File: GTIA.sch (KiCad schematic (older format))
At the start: 78 parts, among them J102 pin, J103 pin, J104 pin, J105 pin, J2 Video, J202 Diag, J210 Diag, Q1 2N3904, Q2 2N3904, Q3 2N3904, Q6 2N3904, U17 GTIA, U18 74LS08, U20 4050, U21 74LS74, Y2 4,43 MHz

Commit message: Basic smd
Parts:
- removed R205: 150, Atari:R_Axial_DIN0207_L3.6mm_D2.2mm_P10.16mm_Horizontal, symbol Device:R
- added D1000: 1N4002, Diode_THT:D_DO-41_SOD81_P12.70mm_Horizontal, symbol Diode:1N4002
- C42: footprint Atari:C_Axial_L5.1mm_D2.5mm_P12.50mm_Horizontal -> Capacitor_SMD:C_1206_3216Metric_Pad1.42x1.75mm_HandSolder
- C50: value 10uF -> 220uF
- R116: value 51 -> 8,2
- R202: value 180 -> 75
- R204: value 47 -> 75
- R53: value 100 -> 75
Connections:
- net at Q2.1 (E), R202.2: now also D1000.2 (A)
- net at FB31.2: now also D1000.1 (K)
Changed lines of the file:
@@
 F 0 "C42" H 4840 4771 50  0000 L CNN
 F 1 "100nF" H 4840 4680 50  0000 L CNN
-F 2 "Atari:C_Axial_L5.1mm_D2.5mm_P12.50mm_Horizontal" H 4763 4575 50  0001 C CNN
+F 2 "Capacitor_SMD:C_1206_3216Metric_Pad1.42x1.75mm_HandSolder" H 4763 4575 50  0001 C CNN
 F 3 "~" H 4725 4725 50  0001 C CNN
 	1    4725 4725
@@
 P 7425 850
 F 0 "C50" H 7543 896 50  0000 L CNN
-F 1 "10uF" H 7543 805 50  0000 L CNN
+F 1 "220uF" H 7543 805 50  0000 L CNN
 F 2 "Capacitor_THT:CP_Radial_D5.0mm_P2.00mm" H 7463 700 50  0001 C CNN
 F 3 "~" H 7425 850 50  0001 C CNN
@@
 P 9300 1125
 F 0 "R116" V 9225 1025 50  0000 L CNN
-F 1 "51" H 9350 1125 50  0000 L CNN
+F 1 "8,2" H 9350 1125 50  0000 L CNN
 F 2 "Atari:R_Axial_DIN0207_L3.6mm_D2.2mm_P10.16mm_Horizontal" V 9230 1125 50  0001 C CNN
 F 3 "~" H 9300 1125 50  0001 C CNN
@@
 P 9300 2125
 F 0 "R53" V 9300 2050 50  0000 L CNN
-F 1 "100" H 9350 2125 50  0000 L CNN
+F 1 "75" H 9350 2125 50  0000 L CNN
 F 2 "Atari:R_Axial_DIN0207_L3.6mm_D2.2mm_P10.16mm_Horizontal" V 9230 2125 50  0001 C CNN
 F 3 "~" H 9300 2125 50  0001 C CNN
@@
 P 9825 1900
 F 0 "R204" V 9750 1900 50  0000 C CNN
-F 1 "47" V 9925 1900 50  0000 C CNN
+F 1 "75" V 9925 1900 50  0000 C CNN
 F 2 "Atari:R_Axial_DIN0207_L3.6mm_D2.2mm_P10.16mm_Horizontal" V 9755 1900 50  0001 C CNN
 F 3 "~" H 9825 1900 50  0001 C CNN
@@
 P 8025 3950
 F 0 "R202" V 8025 3950 50  0000 C CNN
-F 1 "180" V 7909 3950 50  0000 C CNN
+F 1 "75" V 7909 3950 50  0000 C CNN
 F 2 "Atari:R_Axial_DIN0207_L3.6mm_D2.2mm_P10.16mm_Horizontal" V 7955 3950 50  0001 C CNN
 F 3 "~" H 8025 3950 50  0001 C CNN
 	1    8025 3950
 	-1   0    0    1
-$EndComp
-$Comp
-L Device:R R205
-U 1 1 604741B6
-P 8450 3625
-F 0 "R205" V 8450 3625 50  0000 C CNN
-F 1 "150" V 8334 3625 50  0000 C CNN
-F 2 "Atari:R_Axial_DIN0207_L3.6mm_D2.2mm_P10.16mm_Horizontal" V 8380 3625 50  0001 C CNN
-F 3 "~" H 8450 3625 50  0001 C CNN
-	1    8450 3625
-	0    1    1    0
 $EndComp
 Wire Wire Line
@@
 Wire Wire Line
 	3350 7300 3350 7500
+$Comp
+L Diode:1N4002 D1000
+U 1 1 623E583A
+P 8450 3625
+F 0 "D1000" H 8450 3409 50  0000 C CNN
+F 1 "1N4002" H 8450 3500 50  0000 C CNN
+F 2 "Diode_THT:D_DO-41_SOD81_P12.70mm_Horizontal" H 8450 3450 50  0001 C CNN
+F 3 "http://www.vishay.com/docs/88503/1n4001.pdf" H 8450 3625 50  0001 C CNN
+	1    8450 3625
+	-1   0    0    1
+$EndComp
 $EndSCHEMATC

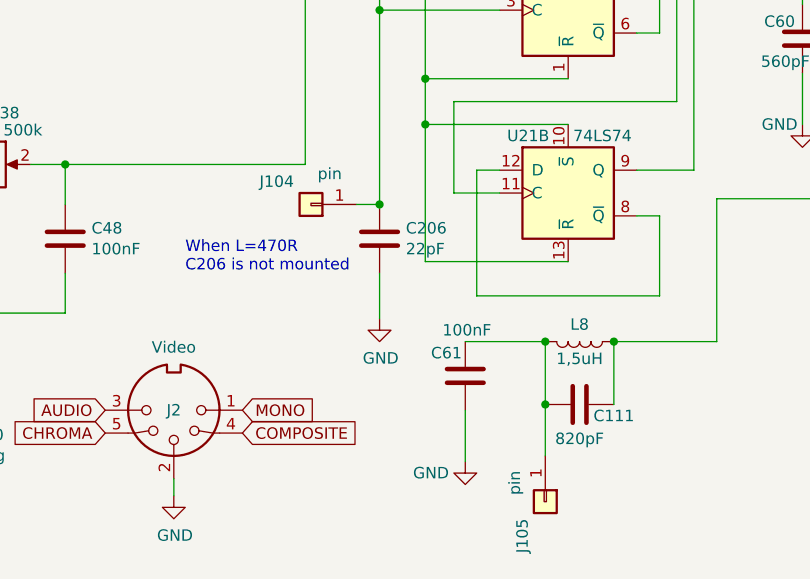
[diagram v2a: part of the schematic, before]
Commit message: PAL to smd
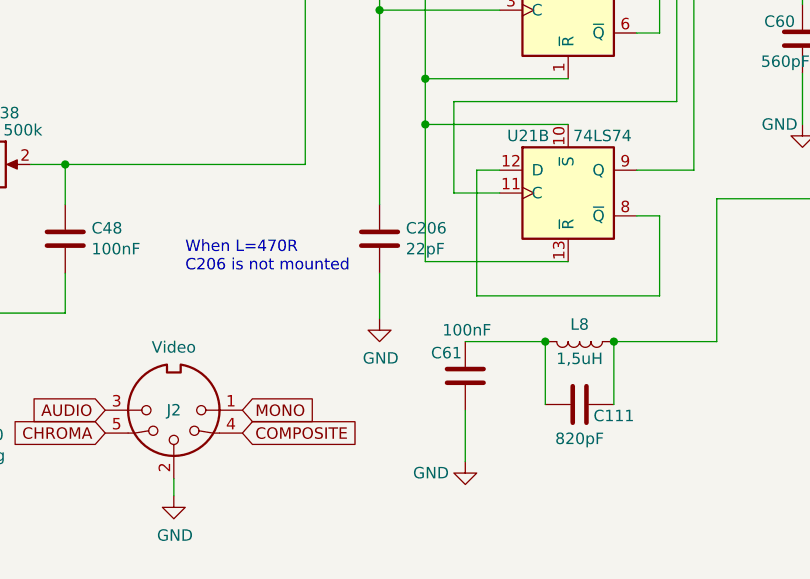
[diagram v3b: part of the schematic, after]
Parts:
- removed J104, J105: pin, Connector_PinHeader_2.00mm:PinHeader_1x01_P2.00mm_Vertical, symbol Connector_Generic:Conn_01x01
- C111, C206, C58, C59, C60, C61: footprint Atari:C_Axial_L5.1mm_D2.5mm_P12.50mm_Horizontal -> Capacitor_SMD:C_1206_3216Metric_Pad1.42x1.75mm_HandSolder
- L37: footprint Atari:L_Axial_L7.0mm_D3.3mm_P12.50mm_Horizontal_Fastron_MICC -> Capacitor_SMD:C_1206_3216Metric_Pad1.42x1.75mm_HandSolder
- L8: footprint Atari:L_Axial_L7.0mm_D3.3mm_P12.50mm_Horizontal_Fastron_MICC -> Inductor_SMD:L_1812_4532Metric_Pad1.30x3.40mm_HandSolder
- R69, R70, R71, R72, R73: footprint Atari:R_Axial_DIN0207_L3.6mm_D2.2mm_P10.16mm_Horizontal -> Resistor_SMD:R_1206_3216Metric_Pad1.42x1.75mm_HandSolder
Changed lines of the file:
@@
 F 0 "C206" H 5310 6354 50  0000 R CNN
 F 1 "22pF" H 5310 6445 50  0000 R CNN
-F 2 "Atari:C_Axial_L5.1mm_D2.5mm_P12.50mm_Horizontal" H 5463 6250 50  0001 C CNN
+F 2 "Capacitor_SMD:C_1206_3216Metric_Pad1.42x1.75mm_HandSolder" H 5463 6250 50  0001 C CNN
 F 3 "~" H 5425 6400 50  0001 C CNN
 	1    5425 6400
@@
 F 0 "L37" V 3725 5200 50  0000 C CNN
 F 1 "Bead or 470R" V 3900 5200 50  0000 C CNN
-F 2 "Atari:L_Axial_L7.0mm_D3.3mm_P12.50mm_Horizontal_Fastron_MICC" H 3800 5200 50  0001 C CNN
+F 2 "Capacitor_SMD:C_1206_3216Metric_Pad1.42x1.75mm_HandSolder" H 3800 5200 50  0001 C CNN
 F 3 "~" H 3800 5200 50  0001 C CNN
 	1    3800 5200
@@
 F 0 "R73" H 7345 5021 50  0000 L CNN
 F 1 "4k7" H 7345 4930 50  0000 L CNN
-F 2 "Atari:R_Axial_DIN0207_L3.6mm_D2.2mm_P10.16mm_Horizontal" V 7205 4975 50  0001 C CNN
+F 2 "Resistor_SMD:R_1206_3216Metric_Pad1.42x1.75mm_HandSolder" V 7205 4975 50  0001 C CNN
 F 3 "~" H 7275 4975 50  0001 C CNN
 	1    7275 4975
@@
 F 0 "C60" H 7375 5450 50  0000 C CNN
 F 1 "560pF" H 7350 5625 50  0000 C CNN
-F 2 "Atari:C_Axial_L5.1mm_D2.5mm_P12.50mm_Horizontal" H 7313 5375 50  0001 C CNN
+F 2 "Capacitor_SMD:C_1206_3216Metric_Pad1.42x1.75mm_HandSolder" H 7313 5375 50  0001 C CNN
 F 3 "~" H 7275 5525 50  0001 C CNN
 	1    7275 5525
@@
 F 0 "C59" V 7850 5250 50  0000 C CNN
 F 1 "22pF" V 7550 5250 50  0000 C CNN
-F 2 "Atari:C_Axial_L5.1mm_D2.5mm_P12.50mm_Horizontal" H 7738 5100 50  0001 C CNN
+F 2 "Capacitor_SMD:C_1206_3216Metric_Pad1.42x1.75mm_HandSolder" H 7738 5100 50  0001 C CNN
 F 3 "~" H 7700 5250 50  0001 C CNN
 	1    7700 5250
@@
 F 0 "R70" H 9445 4996 50  0000 L CNN
 F 1 "10k" H 9445 4905 50  0000 L CNN
-F 2 "Atari:R_Axial_DIN0207_L3.6mm_D2.2mm_P10.16mm_Horizontal" V 9305 4950 50  0001 C CNN
+F 2 "Resistor_SMD:R_1206_3216Metric_Pad1.42x1.75mm_HandSolder" V 9305 4950 50  0001 C CNN
 F 3 "~" H 9375 4950 50  0001 C CNN
 	1    9375 4950
@@
 F 0 "R69" H 9445 5571 50  0000 L CNN
 F 1 "6k8" H 9445 5480 50  0000 L CNN
-F 2 "Atari:R_Axial_DIN0207_L3.6mm_D2.2mm_P10.16mm_Horizontal" V 9305 5525 50  0001 C CNN
+F 2 "Resistor_SMD:R_1206_3216Metric_Pad1.42x1.75mm_HandSolder" V 9305 5525 50  0001 C CNN
 F 3 "~" H 9375 5525 50  0001 C CNN
 	1    9375 5525
@@
 F 0 "R71" V 8868 5250 50  0000 C CNN
 F 1 "470" V 8959 5250 50  0000 C CNN
-F 2 "Atari:R_Axial_DIN0207_L3.6mm_D2.2mm_P10.16mm_Horizontal" V 9005 5250 50  0001 C CNN
+F 2 "Resistor_SMD:R_1206_3216Metric_Pad1.42x1.75mm_HandSolder" V 9005 5250 50  0001 C CNN
 F 3 "~" H 9075 5250 50  0001 C CNN
 	1    9075 5250
@@
 F 0 "R72" V 9568 4425 50  0000 C CNN
 F 1 "1k" V 9659 4425 50  0000 C CNN
-F 2 "Atari:R_Axial_DIN0207_L3.6mm_D2.2mm_P10.16mm_Horizontal" V 9705 4425 50  0001 C CNN
+F 2 "Resistor_SMD:R_1206_3216Metric_Pad1.42x1.75mm_HandSolder" V 9705 4425 50  0001 C CNN
 F 3 "~" H 9775 4425 50  0001 C CNN
 	1    9775 4425
@@
 F 0 "L8" V 6225 6850 50  0000 C CNN
 F 1 "1,5uH" V 6375 6850 50  0000 C CNN
-F 2 "Atari:L_Axial_L7.0mm_D3.3mm_P12.50mm_Horizontal_Fastron_MICC" H 6300 6850 50  0001 C CNN
+F 2 "Inductor_SMD:L_1812_4532Metric_Pad1.30x3.40mm_HandSolder" H 6300 6850 50  0001 C CNN
 F 3 "~" H 6300 6850 50  0001 C CNN
 	1    6300 6850
@@
 F 0 "C111" V 6350 7275 50  0000 C CNN
 F 1 "820pF" V 6450 7125 50  0000 C CNN
-F 2 "Atari:C_Axial_L5.1mm_D2.5mm_P12.50mm_Horizontal" H 6338 6975 50  0001 C CNN
+F 2 "Capacitor_SMD:C_1206_3216Metric_Pad1.42x1.75mm_HandSolder" H 6338 6975 50  0001 C CNN
 F 3 "~" H 6300 7125 50  0001 C CNN
 	1    6300 7125
@@
 F 0 "C61" H 5950 6900 50  0000 R CNN
 F 1 "100nF" H 5900 6800 50  0000 R CNN
-F 2 "Atari:C_Axial_L5.1mm_D2.5mm_P12.50mm_Horizontal" H 5838 6850 50  0001 C CNN
+F 2 "Capacitor_SMD:C_1206_3216Metric_Pad1.42x1.75mm_HandSolder" H 5838 6850 50  0001 C CNN
 F 3 "~" H 5800 7000 50  0001 C CNN
 	1    5800 7000
@@
 F 0 "C58" H 1790 3671 50  0000 L CNN
 F 1 "100nF" H 1790 3580 50  0000 L CNN
-F 2 "Atari:C_Axial_L5.1mm_D2.5mm_P12.50mm_Horizontal" H 1713 3475 50  0001 C CNN
+F 2 "Capacitor_SMD:C_1206_3216Metric_Pad1.42x1.75mm_HandSolder" H 1713 3475 50  0001 C CNN
 F 3 "~" H 1675 3625 50  0001 C CNN
 	1    1675 3625
@@
 Wire Wire Line
 	2375 6200 2375 6000
-$Comp
-L Connector_Generic:Conn_01x01 J104
-U 1 1 603FEA4A
-P 5125 6250
-F 0 "J104" H 5275 6150 50  0000 C CNN
-F 1 "pin" H 5043 6116 50  0000 C CNN
-F 2 "Connector_PinHeader_2.00mm:PinHeader_1x01_P2.00mm_Vertical" H 5125 6250 50  0001 C CNN
-F 3 "~" H 5125 6250 50  0001 C CNN
-	1    5125 6250
-	-1   0    0    1
-$EndComp
-Wire Wire Line
-	5325 6250 5425 6250
-Connection ~ 5425 6250
-$Comp
-L Connector_Generic:Conn_01x01 J105
-U 1 1 6041A994
-P 6150 7550
-F 0 "J105" H 6300 7450 50  0000 C CNN
-F 1 "pin" H 6068 7416 50  0000 C CNN
-F 2 "Connector_PinHeader_2.00mm:PinHeader_1x01_P2.00mm_Vertical" H 6150 7550 50  0001 C CNN
-F 3 "~" H 6150 7550 50  0001 C CNN
-	1    6150 7550
-	0    1    1    0
-$EndComp
-Wire Wire Line
-	6150 7350 6150 7125
-Connection ~ 6150 7125
 Text GLabel 2650 7200 0    50   Input ~ 0
 MONO

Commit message: ROM refactoring
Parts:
- removed J102, J103: pin, Connector_PinHeader_2.00mm:PinHeader_1x01_P2.00mm_Vertical, symbol Connector_Generic:Conn_01x01
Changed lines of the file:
@@
 	1    0    0    -1
 $EndComp
-$Comp
-L Connector_Generic:Conn_01x01 J102
-U 1 1 6037C604
-P 800 6575
-F 0 "J102" H 950 6475 50  0000 C CNN
-F 1 "pin" H 718 6441 50  0000 C CNN
-F 2 "Connector_PinHeader_2.00mm:PinHeader_1x01_P2.00mm_Vertical" H 800 6575 50  0001 C CNN
-F 3 "~" H 800 6575 50  0001 C CNN
-	1    800  6575
-	-1   0    0    1
-$EndComp
-Wire Wire Line
-	1000 6575 1200 6575
-Wire Wire Line
-	1200 6575 1200 6200
-$Comp
-L Connector_Generic:Conn_01x01 J103
-U 1 1 603DC950
-P 2375 6400
-F 0 "J103" H 2525 6300 50  0000 C CNN
-F 1 "pin" H 2293 6266 50  0000 C CNN
-F 2 "Connector_PinHeader_2.00mm:PinHeader_1x01_P2.00mm_Vertical" H 2375 6400 50  0001 C CNN
-F 3 "~" H 2375 6400 50  0001 C CNN
-	1    2375 6400
-	0    1    1    0
-$EndComp
-Wire Wire Line
-	2375 6200 2375 6000
 Text GLabel 2650 7200 0    50   Input ~ 0
 MONO

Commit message: SMD continue
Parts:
- C204, C51: footprint Atari:C_Axial_L5.1mm_D2.5mm_P12.50mm_Horizontal -> Capacitor_SMD:C_1206_3216Metric_Pad1.42x1.75mm_HandSolder
- D1000: footprint Diode_THT:D_DO-41_SOD81_P12.70mm_Horizontal -> Diode_SMD:D_MELF_Handsoldering
- FB31, L32, L5, L6: footprint Atari:L_Axial_L7.0mm_D3.3mm_P12.50mm_Horizontal_Fastron_MICC -> Inductor_SMD:L_1812_4532Metric_Pad1.30x3.40mm_HandSolder
- R201, R202, R203, R41, R42, R43, R44, R45: footprint Atari:R_Axial_DIN0207_L3.6mm_D2.2mm_P10.16mm_Horizontal -> Resistor_SMD:R_1206_3216Metric_Pad1.42x1.75mm_HandSolder
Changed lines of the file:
@@
 F 0 "R41" V 6225 1100 50  0000 L CNN
 F 1 "1k" H 6275 1175 50  0000 L CNN
-F 2 "Atari:R_Axial_DIN0207_L3.6mm_D2.2mm_P10.16mm_Horizontal" V 6155 1175 50  0001 C CNN
+F 2 "Resistor_SMD:R_1206_3216Metric_Pad1.42x1.75mm_HandSolder" V 6155 1175 50  0001 C CNN
 F 3 "~" H 6225 1175 50  0001 C CNN
 	1    6225 1175
@@
 F 0 "R42" V 6025 1100 50  0000 L CNN
 F 1 "1k" H 6075 1175 50  0000 L CNN
-F 2 "Atari:R_Axial_DIN0207_L3.6mm_D2.2mm_P10.16mm_Horizontal" V 5955 1175 50  0001 C CNN
+F 2 "Resistor_SMD:R_1206_3216Metric_Pad1.42x1.75mm_HandSolder" V 5955 1175 50  0001 C CNN
 F 3 "~" H 6025 1175 50  0001 C CNN
 	1    6025 1175
@@
 F 0 "R43" V 5825 1100 50  0000 L CNN
 F 1 "1k" H 5875 1175 50  0000 L CNN
-F 2 "Atari:R_Axial_DIN0207_L3.6mm_D2.2mm_P10.16mm_Horizontal" V 5755 1175 50  0001 C CNN
+F 2 "Resistor_SMD:R_1206_3216Metric_Pad1.42x1.75mm_HandSolder" V 5755 1175 50  0001 C CNN
 F 3 "~" H 5825 1175 50  0001 C CNN
 	1    5825 1175
@@
 F 0 "R44" V 5625 1100 50  0000 L CNN
 F 1 "1k" H 5675 1175 50  0000 L CNN
-F 2 "Atari:R_Axial_DIN0207_L3.6mm_D2.2mm_P10.16mm_Horizontal" V 5555 1175 50  0001 C CNN
+F 2 "Resistor_SMD:R_1206_3216Metric_Pad1.42x1.75mm_HandSolder" V 5555 1175 50  0001 C CNN
 F 3 "~" H 5625 1175 50  0001 C CNN
 	1    5625 1175
@@
 F 0 "R45" V 5425 1100 50  0000 L CNN
 F 1 "1k" H 5475 1175 50  0000 L CNN
-F 2 "Atari:R_Axial_DIN0207_L3.6mm_D2.2mm_P10.16mm_Horizontal" V 5355 1175 50  0001 C CNN
+F 2 "Resistor_SMD:R_1206_3216Metric_Pad1.42x1.75mm_HandSolder" V 5355 1175 50  0001 C CNN
 F 3 "~" H 5425 1175 50  0001 C CNN
 	1    5425 1175
@@
 F 0 "L5" V 6750 700 50  0000 C CNN
 F 1 "820uH" V 6900 700 50  0000 C CNN
-F 2 "Atari:L_Axial_L7.0mm_D3.3mm_P12.50mm_Horizontal_Fastron_MICC" H 6825 700 50  0001 C CNN
+F 2 "Inductor_SMD:L_1812_4532Metric_Pad1.30x3.40mm_HandSolder" H 6825 700 50  0001 C CNN
 F 3 "~" H 6825 700 50  0001 C CNN
 	1    6825 700
@@
 F 0 "C51" H 8865 896 50  0000 L CNN
 F 1 "100nF" H 8865 805 50  0000 L CNN
-F 2 "Atari:C_Axial_L5.1mm_D2.5mm_P12.50mm_Horizontal" H 8788 700 50  0001 C CNN
+F 2 "Capacitor_SMD:C_1206_3216Metric_Pad1.42x1.75mm_HandSolder" H 8788 700 50  0001 C CNN
 F 3 "~" H 8750 850 50  0001 C CNN
 	1    8750 850
@@
 F 0 "R203" V 7075 3075 50  0000 C CNN
 F 1 "3k3" V 6959 3075 50  0000 C CNN
-F 2 "Atari:R_Axial_DIN0207_L3.6mm_D2.2mm_P10.16mm_Horizontal" V 7005 3075 50  0001 C CNN
+F 2 "Resistor_SMD:R_1206_3216Metric_Pad1.42x1.75mm_HandSolder" V 7005 3075 50  0001 C CNN
 F 3 "~" H 7075 3075 50  0001 C CNN
 	1    7075 3075
@@
 F 0 "R201" V 7250 3375 50  0000 C CNN
 F 1 "6k8" V 7134 3375 50  0000 C CNN
-F 2 "Atari:R_Axial_DIN0207_L3.6mm_D2.2mm_P10.16mm_Horizontal" V 7180 3375 50  0001 C CNN
+F 2 "Resistor_SMD:R_1206_3216Metric_Pad1.42x1.75mm_HandSolder" V 7180 3375 50  0001 C CNN
 F 3 "~" H 7250 3375 50  0001 C CNN
 	1    7250 3375
@@
 F 0 "L6" V 6800 3375 50  0000 C CNN
 F 1 "100uH" V 6950 3375 50  0000 C CNN
-F 2 "Atari:L_Axial_L7.0mm_D3.3mm_P12.50mm_Horizontal_Fastron_MICC" H 6875 3375 50  0001 C CNN
+F 2 "Inductor_SMD:L_1812_4532Metric_Pad1.30x3.40mm_HandSolder" H 6875 3375 50  0001 C CNN
 F 3 "~" H 6875 3375 50  0001 C CNN
 	1    6875 3375
@@
 F 0 "L32" V 7500 3075 50  0000 C CNN
 F 1 "100uH" V 7525 3300 50  0000 C CNN
-F 2 "Atari:L_Axial_L7.0mm_D3.3mm_P12.50mm_Horizontal_Fastron_MICC" H 7575 3075 50  0001 C CNN
+F 2 "Inductor_SMD:L_1812_4532Metric_Pad1.30x3.40mm_HandSolder" H 7575 3075 50  0001 C CNN
 F 3 "~" H 7575 3075 50  0001 C CNN
 	1    7575 3075
@@
 F 0 "R202" V 8025 3950 50  0000 C CNN
 F 1 "75" V 7909 3950 50  0000 C CNN
-F 2 "Atari:R_Axial_DIN0207_L3.6mm_D2.2mm_P10.16mm_Horizontal" V 7955 3950 50  0001 C CNN
+F 2 "Resistor_SMD:R_1206_3216Metric_Pad1.42x1.75mm_HandSolder" V 7955 3950 50  0001 C CNN
 F 3 "~" H 8025 3950 50  0001 C CNN
 	1    8025 3950
@@
 F 0 "FB31" V 8750 3650 50  0000 C CNN
 F 1 "Ferrite_Bead" V 8850 3950 50  0000 C CNN
-F 2 "Atari:L_Axial_L7.0mm_D3.3mm_P12.50mm_Horizontal_Fastron_MICC" V 8855 3625 50  0001 C CNN
+F 2 "Inductor_SMD:L_1812_4532Metric_Pad1.30x3.40mm_HandSolder" V 8855 3625 50  0001 C CNN
 F 3 "~" H 8925 3625 50  0001 C CNN
 	1    8925 3625
@@
 F 0 "C204" H 7725 3875 50  0000 C CNN
 F 1 "100nF" H 7700 4050 50  0000 C CNN
-F 2 "Atari:C_Axial_L5.1mm_D2.5mm_P12.50mm_Horizontal" H 7663 3800 50  0001 C CNN
+F 2 "Capacitor_SMD:C_1206_3216Metric_Pad1.42x1.75mm_HandSolder" H 7663 3800 50  0001 C CNN
 F 3 "~" H 7625 3950 50  0001 C CNN
 	1    7625 3950
@@
 F 0 "D1000" H 8450 3409 50  0000 C CNN
 F 1 "1N4002" H 8450 3500 50  0000 C CNN
-F 2 "Diode_THT:D_DO-41_SOD81_P12.70mm_Horizontal" H 8450 3450 50  0001 C CNN
+F 2 "Diode_SMD:D_MELF_Handsoldering" H 8450 3450 50  0001 C CNN
 F 3 "http://www.vishay.com/docs/88503/1n4001.pdf" H 8450 3625 50  0001 C CNN
 	1    8450 3625

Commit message: SMD continue
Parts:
- C44, C45, C46, C47, C48: footprint Atari:C_Axial_L5.1mm_D2.5mm_P12.50mm_Horizontal -> Capacitor_SMD:C_1206_3216Metric_Pad1.42x1.75mm_HandSolder
- D2, D3, D4: footprint Diode_THT:D_DO-35_SOD27_P12.70mm_Horizontal -> Diode_SMD:D_MiniMELF
- R116, R35, R36, R37, R46, R47, R48, R49, R50, R51: footprint Atari:R_Axial_DIN0207_L3.6mm_D2.2mm_P10.16mm_Horizontal -> Resistor_SMD:R_1206_3216Metric_Pad1.42x1.75mm_HandSolder
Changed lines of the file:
@@
 F 0 "C44" V 648 6200 50  0000 C CNN
 F 1 "68pF" V 739 6200 50  0000 C CNN
-F 2 "Atari:C_Axial_L5.1mm_D2.5mm_P12.50mm_Horizontal" H 938 6050 50  0001 C CNN
+F 2 "Capacitor_SMD:C_1206_3216Metric_Pad1.42x1.75mm_HandSolder" H 938 6050 50  0001 C CNN
 F 3 "~" H 900 6200 50  0001 C CNN
 	1    900  6200
@@
 F 0 "R35" H 1270 5721 50  0000 L CNN
 F 1 "33k" H 1270 5630 50  0000 L CNN
-F 2 "Atari:R_Axial_DIN0207_L3.6mm_D2.2mm_P10.16mm_Horizontal" V 1130 5675 50  0001 C CNN
+F 2 "Resistor_SMD:R_1206_3216Metric_Pad1.42x1.75mm_HandSolder" V 1130 5675 50  0001 C CNN
 F 3 "~" H 1200 5675 50  0001 C CNN
 	1    1200 5675
@@
 F 0 "R36" H 1670 5721 50  0000 L CNN
 F 1 "680" H 1670 5630 50  0000 L CNN
-F 2 "Atari:R_Axial_DIN0207_L3.6mm_D2.2mm_P10.16mm_Horizontal" V 1530 5675 50  0001 C CNN
+F 2 "Resistor_SMD:R_1206_3216Metric_Pad1.42x1.75mm_HandSolder" V 1530 5675 50  0001 C CNN
 F 3 "~" H 1600 5675 50  0001 C CNN
 	1    1600 5675
@@
 F 0 "C45" V 1950 6125 50  0000 C CNN
 F 1 "220pF" V 1864 6000 50  0000 C CNN
-F 2 "Atari:C_Axial_L5.1mm_D2.5mm_P12.50mm_Horizontal" H 2063 5850 50  0001 C CNN
+F 2 "Capacitor_SMD:C_1206_3216Metric_Pad1.42x1.75mm_HandSolder" H 2063 5850 50  0001 C CNN
 F 3 "~" H 2025 6000 50  0001 C CNN
 	1    2025 6000
@@
 F 0 "D2" V 2450 5825 50  0000 R CNN
 F 1 "1N4148" V 2450 5600 50  0000 R CNN
-F 2 "Diode_THT:D_DO-35_SOD27_P12.70mm_Horizontal" H 2375 5500 50  0001 C CNN
+F 2 "Diode_SMD:D_MiniMELF" H 2375 5500 50  0001 C CNN
 F 3 "https://assets.nexperia.com/documents/data-sheet/1N4148_1N4448.pdf" H 2375 5675 50  0001 C CNN
 	1    2375 5675
@@
 F 0 "D3" H 2550 5950 50  0000 C CNN
 F 1 "1N4148" H 2675 5875 50  0000 C CNN
-F 2 "Diode_THT:D_DO-35_SOD27_P12.70mm_Horizontal" H 2675 5825 50  0001 C CNN
+F 2 "Diode_SMD:D_MiniMELF" H 2675 5825 50  0001 C CNN
 F 3 "https://assets.nexperia.com/documents/data-sheet/1N4148_1N4448.pdf" H 2675 6000 50  0001 C CNN
 	1    2675 6000
@@
 F 0 "C46" H 3075 6325 50  0000 C CNN
 F 1 "1nF" H 3050 6500 50  0000 C CNN
-F 2 "Atari:C_Axial_L5.1mm_D2.5mm_P12.50mm_Horizontal" H 3013 6250 50  0001 C CNN
+F 2 "Capacitor_SMD:C_1206_3216Metric_Pad1.42x1.75mm_HandSolder" H 3013 6250 50  0001 C CNN
 F 3 "~" H 2975 6400 50  0001 C CNN
 	1    2975 6400
@@
 F 0 "C47" H 3425 6325 50  0000 C CNN
 F 1 "1nF" H 3400 6500 50  0000 C CNN
-F 2 "Atari:C_Axial_L5.1mm_D2.5mm_P12.50mm_Horizontal" H 3363 6250 50  0001 C CNN
+F 2 "Capacitor_SMD:C_1206_3216Metric_Pad1.42x1.75mm_HandSolder" H 3363 6250 50  0001 C CNN
 F 3 "~" H 3325 6400 50  0001 C CNN
 	1    3325 6400
@@
 F 0 "R37" V 2943 5750 50  0000 C CNN
 F 1 "1k" V 3034 5750 50  0000 C CNN
-F 2 "Atari:R_Axial_DIN0207_L3.6mm_D2.2mm_P10.16mm_Horizontal" V 3080 5750 50  0001 C CNN
+F 2 "Resistor_SMD:R_1206_3216Metric_Pad1.42x1.75mm_HandSolder" V 3080 5750 50  0001 C CNN
 F 3 "~" H 3150 5750 50  0001 C CNN
 	1    3150 5750
@@
 F 0 "C48" H 3935 6354 50  0000 R CNN
 F 1 "100nF" H 3935 6445 50  0000 R CNN
-F 2 "Atari:C_Axial_L5.1mm_D2.5mm_P12.50mm_Horizontal" H 4088 6250 50  0001 C CNN
+F 2 "Capacitor_SMD:C_1206_3216Metric_Pad1.42x1.75mm_HandSolder" H 4088 6250 50  0001 C CNN
 F 3 "~" H 4050 6400 50  0001 C CNN
 	1    4050 6400
@@
 F 0 "R47" V 7925 1500 50  0000 C CNN
 F 1 "36k" V 7809 1500 50  0000 C CNN
-F 2 "Atari:R_Axial_DIN0207_L3.6mm_D2.2mm_P10.16mm_Horizontal" V 7855 1500 50  0001 C CNN
+F 2 "Resistor_SMD:R_1206_3216Metric_Pad1.42x1.75mm_HandSolder" V 7855 1500 50  0001 C CNN
 F 3 "~" H 7925 1500 50  0001 C CNN
 	1    7925 1500
@@
 F 0 "R48" V 7925 1825 50  0000 C CNN
 F 1 "18k" V 7809 1825 50  0000 C CNN
-F 2 "Atari:R_Axial_DIN0207_L3.6mm_D2.2mm_P10.16mm_Horizontal" V 7855 1825 50  0001 C CNN
+F 2 "Resistor_SMD:R_1206_3216Metric_Pad1.42x1.75mm_HandSolder" V 7855 1825 50  0001 C CNN
 F 3 "~" H 7925 1825 50  0001 C CNN
 	1    7925 1825
@@
 F 0 "R49" V 7925 2150 50  0000 C CNN
 F 1 "9k1" V 7809 2150 50  0000 C CNN
-F 2 "Atari:R_Axial_DIN0207_L3.6mm_D2.2mm_P10.16mm_Horizontal" V 7855 2150 50  0001 C CNN
+F 2 "Resistor_SMD:R_1206_3216Metric_Pad1.42x1.75mm_HandSolder" V 7855 2150 50  0001 C CNN
 F 3 "~" H 7925 2150 50  0001 C CNN
 	1    7925 2150
@@
 F 0 "R50" V 7925 2475 50  0000 C CNN
 F 1 "4k7" V 7809 2475 50  0000 C CNN
-F 2 "Atari:R_Axial_DIN0207_L3.6mm_D2.2mm_P10.16mm_Horizontal" V 7855 2475 50  0001 C CNN
+F 2 "Resistor_SMD:R_1206_3216Metric_Pad1.42x1.75mm_HandSolder" V 7855 2475 50  0001 C CNN
 F 3 "~" H 7925 2475 50  0001 C CNN
 	1    7925 2475
@@
 F 0 "R51" V 8250 2800 50  0000 C CNN
 F 1 "750" V 8134 2800 50  0000 C CNN
-F 2 "Atari:R_Axial_DIN0207_L3.6mm_D2.2mm_P10.16mm_Horizontal" V 8180 2800 50  0001 C CNN
+F 2 "Resistor_SMD:R_1206_3216Metric_Pad1.42x1.75mm_HandSolder" V 8180 2800 50  0001 C CNN
 F 3 "~" H 8250 2800 50  0001 C CNN
 	1    8250 2800
@@
 F 0 "D4" H 7600 2700 50  0000 C CNN
 F 1 "1N4148" H 7600 2925 50  0000 C CNN
-F 2 "Diode_THT:D_DO-35_SOD27_P12.70mm_Horizontal" H 7600 2625 50  0001 C CNN
+F 2 "Diode_SMD:D_MiniMELF" H 7600 2625 50  0001 C CNN
 F 3 "https://assets.nexperia.com/documents/data-sheet/1N4148_1N4448.pdf" H 7600 2800 50  0001 C CNN
 	1    7600 2800
@@
 F 0 "R46" V 8400 1050 50  0000 L CNN
 F 1 "1k6" H 8450 1125 50  0000 L CNN
-F 2 "Atari:R_Axial_DIN0207_L3.6mm_D2.2mm_P10.16mm_Horizontal" V 8330 1125 50  0001 C CNN
+F 2 "Resistor_SMD:R_1206_3216Metric_Pad1.42x1.75mm_HandSolder" V 8330 1125 50  0001 C CNN
 F 3 "~" H 8400 1125 50  0001 C CNN
 	1    8400 1125
@@
 F 0 "R116" V 9225 1025 50  0000 L CNN
 F 1 "8,2" H 9350 1125 50  0000 L CNN
-F 2 "Atari:R_Axial_DIN0207_L3.6mm_D2.2mm_P10.16mm_Horizontal" V 9230 1125 50  0001 C CNN
+F 2 "Resistor_SMD:R_1206_3216Metric_Pad1.42x1.75mm_HandSolder" V 9230 1125 50  0001 C CNN
 F 3 "~" H 9300 1125 50  0001 C CNN
 	1    9300 1125
